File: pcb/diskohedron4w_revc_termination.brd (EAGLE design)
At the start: 87.2 x 55.5 mm, 64 parts

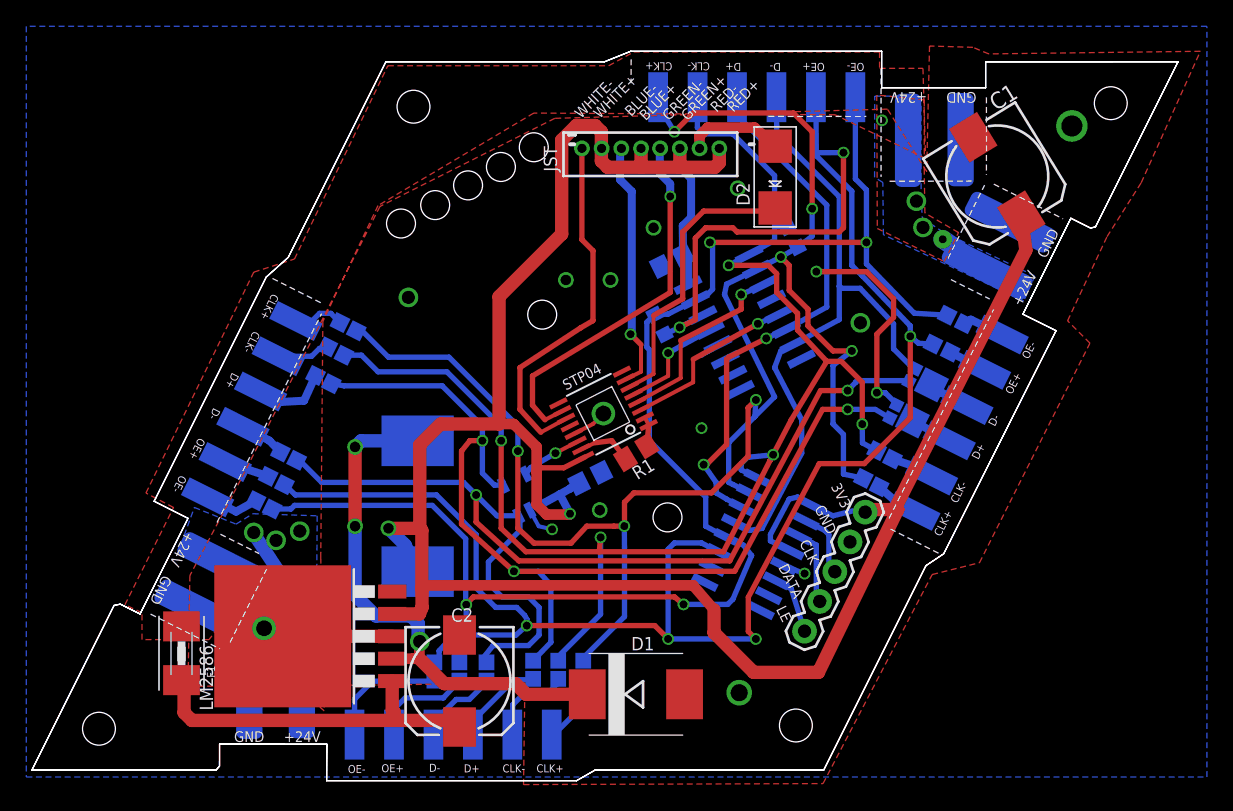
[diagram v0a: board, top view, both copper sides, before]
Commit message: added termination resistors for rev.c & d
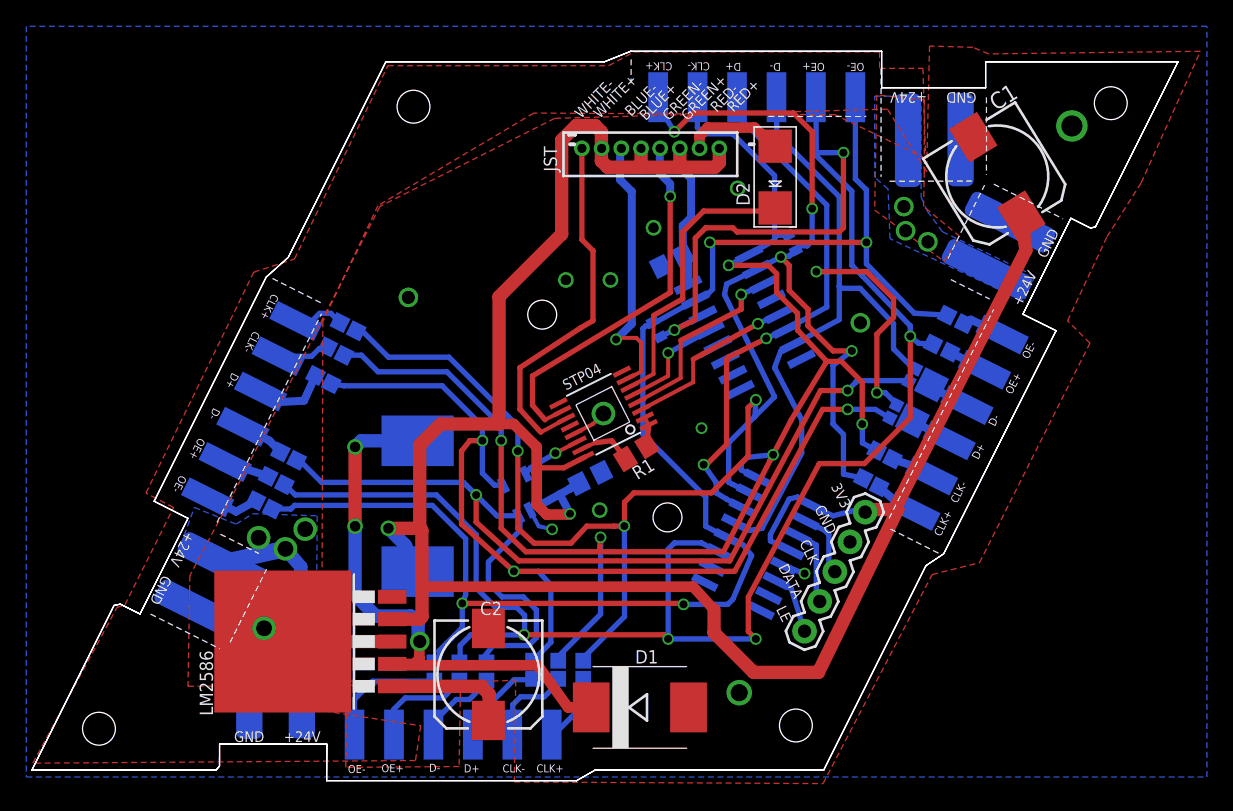
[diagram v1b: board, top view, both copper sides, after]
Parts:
- removed F1: (no value), adafruit:1812
- R2, R3: device rcl:R0603 -> rcl:R0402
- moved C2 2.26 mm to (34.7, 7.30)
- moved D1 1.04 mm to (46.3, 4.79)
- moved R2 0.43 mm to (47.5, 33.6)
- moved R3 0.42 mm to (57.8, 40.1), turned to 243 degrees
- moved LM2586 0.40 mm to (21.6, 9.80)
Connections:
- removed net IN+24V: C2.+, F1.1, LM2586.1
- net +24V: now also C2.+, LM2586.1; no longer F1.2
- net CLK+: now also R3.2; no longer R3.1
- net CLK-: now also R3.1; no longer R3.2
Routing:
- net IN+24V: track 27.0 -> 0.00 mm
- net +24V: track 16.8 -> 25.8 mm, vias 7 -> 6
- net N$2: track 41.0 -> 44.1 mm
- net LED1: track 19.1 -> 21.0 mm
- net OE+: track 144.4 -> 145.3 mm
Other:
- board text added: "06/2014"
- board text added: "rev.C"
- board text removed: "10/2014"
- board text removed: "rev.D"
